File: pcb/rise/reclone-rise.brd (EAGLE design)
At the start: 85 x 56 mm, 130 parts, among them Y1 12MHz

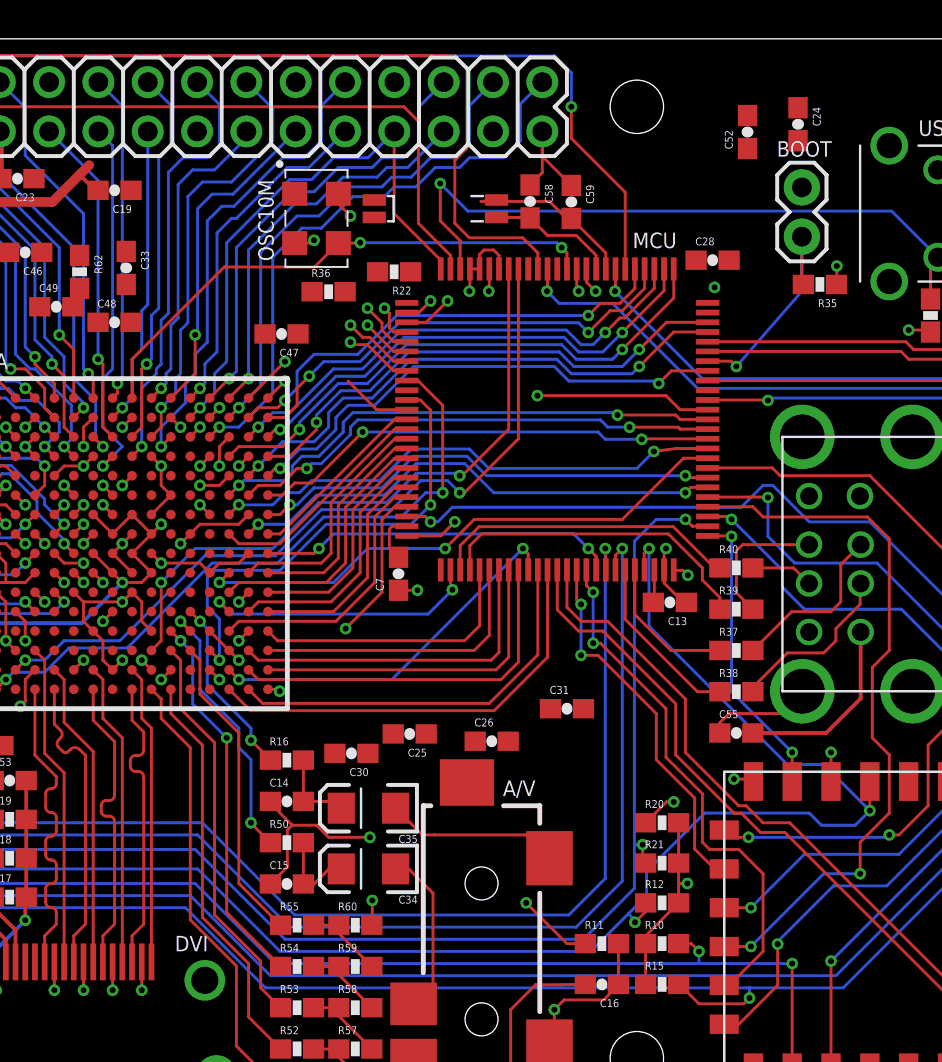
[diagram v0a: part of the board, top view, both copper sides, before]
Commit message: Placed and routed some pull resistors and bypass caps
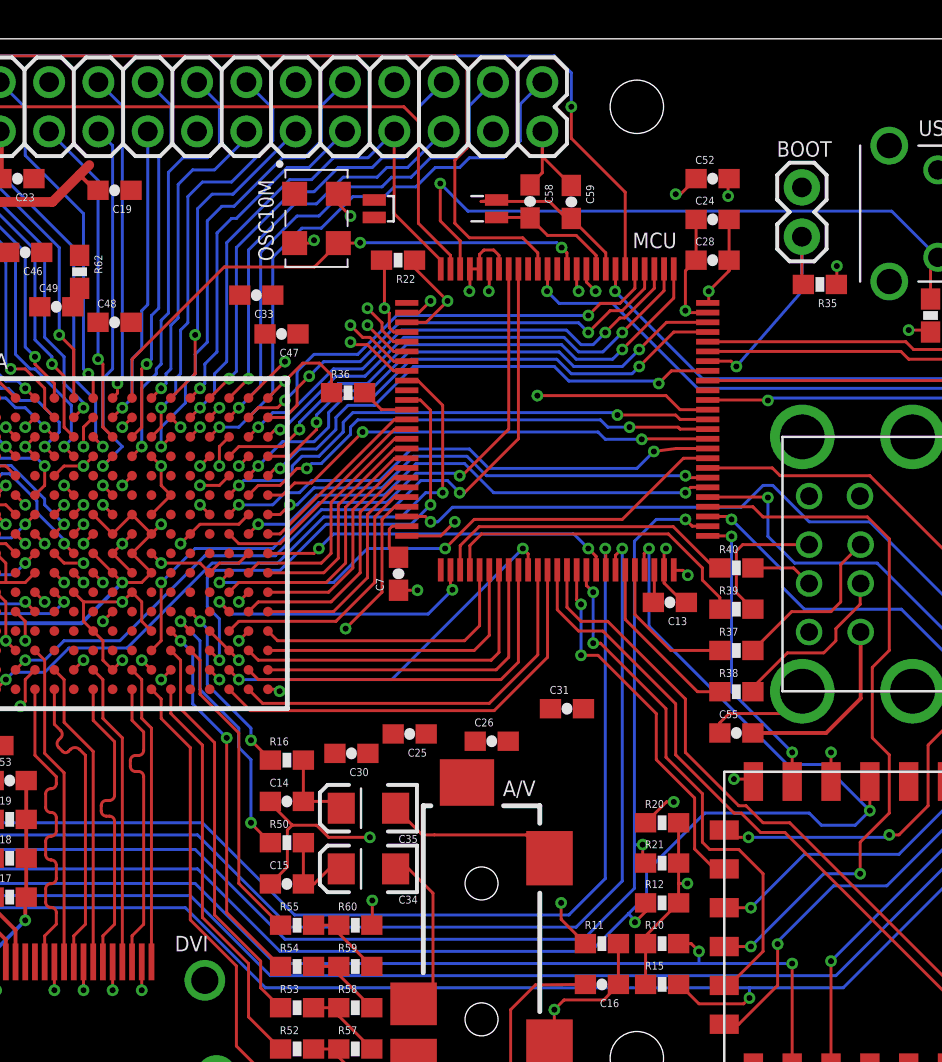
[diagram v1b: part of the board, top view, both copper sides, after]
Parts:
- moved C33 6.84 mm to (41.9, 42.8), turned to 180 degrees
- moved C24 6.59 mm to (65.4, 46.7), turned to 0 degrees
- moved R36 5.30 mm to (46.6, 37.8)
- moved C52 3.00 mm to (65.4, 48.8), turned to 0 degrees
- moved R22 0.63 mm to (49.2, 44.6)
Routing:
- net GND: track 171.4 -> 182.9 mm, vias 59 -> 61
- net +3V3: track 87.6 -> 95.0 mm
- net JTAG_TCK: track 112.9 -> 108.5 mm
- net SD_CS: track 57.6 -> 60.1 mm
- net +5V: track 208.8 -> 210.5 mm, vias 2 -> 3
- net BOOT1: track 3.64 -> 2.54 mm

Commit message: Almost done routing
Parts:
- moved C18 63.9 mm to (82.5, 38.0)
- moved C55 54.6 mm to (19.4, 47.7)
- moved C50 26.7 mm to (37.6, 18.0), turned to 90 degrees
- moved C38 19.0 mm to (21.5, 22.6)
- moved C49 18.8 mm to (24.6, 24.7), turned to 180 degrees
- moved C31 8.89 mm to (66.6, 19.8)
- moved C19 7.81 mm to (26.8, 47.8), turned to 90 degrees
- moved C26 7.56 mm to (46.5, 20.6), turned to 180 degrees
- moved C30 6.96 mm to (49.0, 25.8), turned to 0 degrees
- moved C46 6.08 mm to (36.0, 46.0)
- moved R62 5.86 mm to (27.5, 41.5), turned to 180 degrees
- moved C42 4.63 mm to (21.5, 24.7), turned to 0 degrees
- moved C43 4.48 mm to (20.8, 39.1)
- moved C25 3.71 mm to (46.5, 18.5)
- moved C45 3.42 mm to (24.6, 22.6), turned to 180 degrees
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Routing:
- net GND: track 182.9 -> 227.9 mm, vias 61 -> 76
- net +1V8: track 108.1 -> 134.8 mm
- net +3V3: track 95.0 -> 118.8 mm
- net +5V: track 210.5 -> 196.1 mm, vias 3 -> 4
- net +1V2: track 50.7 -> 56.8 mm, vias 2 -> 4
- net DDR2_VREF: track 57.7 -> 60.6 mm
- net M3A0: track 27.8 -> 26.9 mm
- net M3A9: vias 0 -> 2

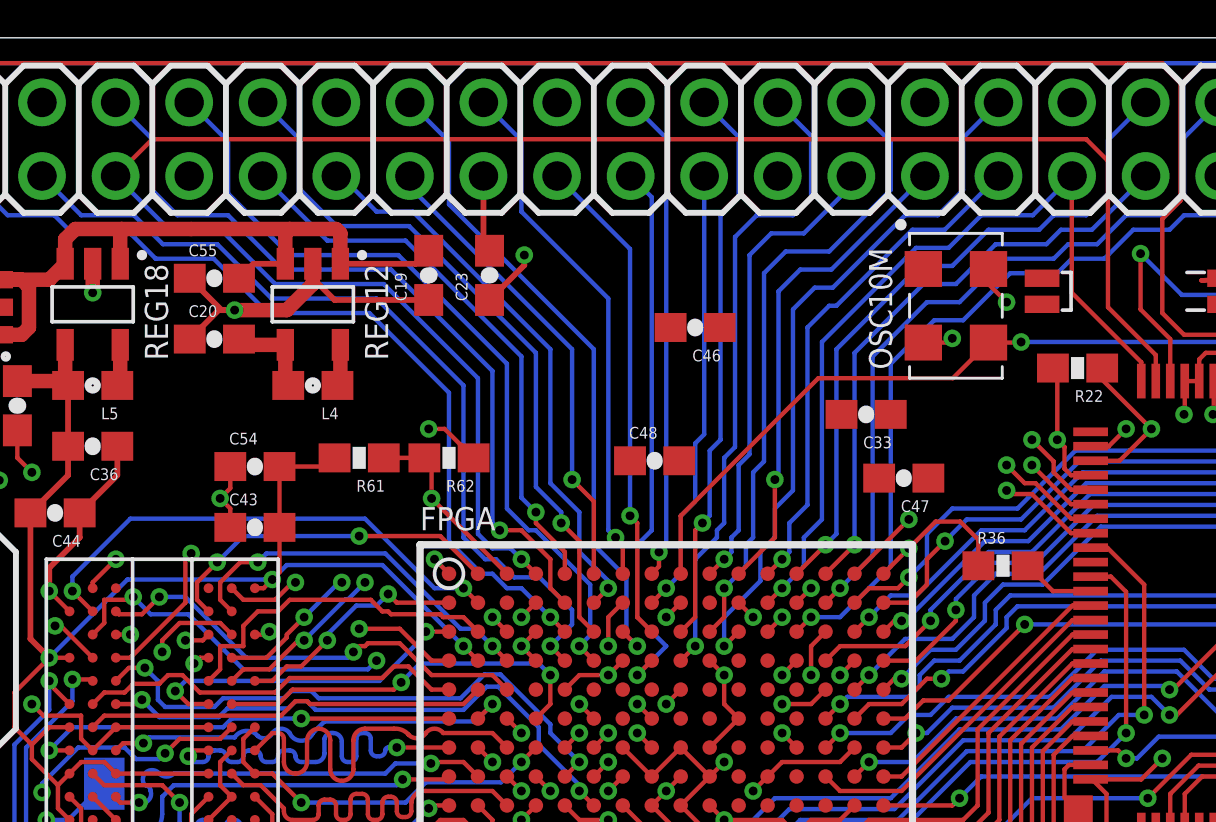
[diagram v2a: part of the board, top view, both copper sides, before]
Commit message: Finished routing first draft
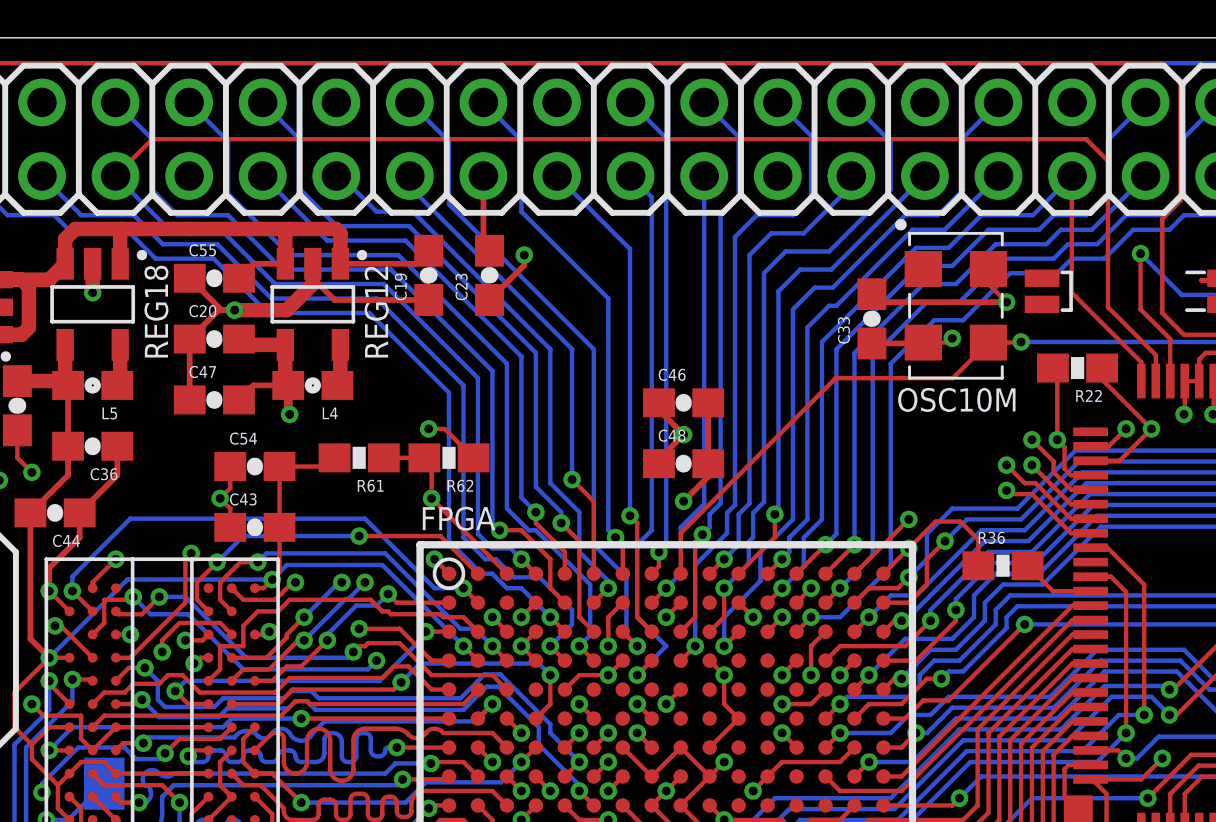
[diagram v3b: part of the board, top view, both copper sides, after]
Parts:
- moved C47 24.0 mm to (19.4, 43.5), turned to 0 degrees
- moved C33 3.31 mm to (42.1, 46.3), turned to 90 degrees
- moved C46 2.63 mm to (35.6, 43.4), turned to 0 degrees
- moved C48 1.00 mm to (35.6, 41.3)
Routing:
- net +1V2: track 56.8 -> 76.1 mm, vias 4 -> 6
- net GND: track 227.9 -> 234.6 mm, vias 76 -> 77
- net +3V3: track 118.8 -> 123.6 mm

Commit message: Fixed a few ERC issues
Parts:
- BAT: value (none) -> 3V
- BOOT: value (none) -> BOOT
- BUSPWR: value (none) -> BUSPWR
- Y4: value (none) -> 32K768
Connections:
- net GPIO25: now also FPGA.D12
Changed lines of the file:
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@@
 <element name="C7" library="SparkFun-Passives" package="0603-CAP" value="2u2" x="49.225" y="28.45" rot="R90"/>
 <element name="C13" library="SparkFun-Passives" package="0603-CAP" value="2u2" x="63.2" y="26.975" rot="R180"/>
-<element name="BOOT" library="SparkFun-Connectors" package="1X02" value="" x="70" y="48.35" locked="yes" smashed="yes" rot="R270">
+<element name="BOOT" library="SparkFun-Connectors" package="1X02" value="BOOT" x="70" y="48.35" locked="yes" smashed="yes" rot="R270">
 <attribute name="NAME" x="68.7038" y="49.9288" size="0.8" layer="25" font="vector" ratio="19"/>
 <attribute name="VALUE" x="66.825" y="49.62" size="1.27" layer="27" rot="R270"/>
 </element>
-<element name="BUSPWR" library="SparkFun-Connectors" package="1X02" value="" x="2" y="20" smashed="yes">
+<element name="BUSPWR" library="SparkFun-Connectors" package="1X02" value="BUSPWR" x="2" y="20" smashed="yes">
 <attribute name="NAME" x="0.6538" y="21.6288" size="0.8" layer="25" font="vector" ratio="19"/>
 <attribute name="VALUE" x="0.73" y="16.825" size="1.27" layer="27"/>
@@
 <element name="C54" library="SparkFun-Passives" package="0603-CAP" value="4u7" x="20.8" y="41.2"/>
 <element name="C55" library="SparkFun-Passives" package="0603-CAP" value="4u7" x="19.4" y="47.7"/>
-<element name="BAT" library="SparkFun-Electromechanical" package="BATTCON_12MM" value="" x="6.2" y="35.2" locked="yes" rot="R90">
+<element name="BAT" library="SparkFun-Electromechanical" package="BATTCON_12MM" value="3V" x="6.2" y="35.2" locked="yes" rot="R90">
 <attribute name="PROD_ID" value="BATT-08044" x="6.2" y="35.2" size="1.778" layer="27" rot="R90" display="off"/>
 </element>
-<element name="Y4" library="SparkFun-FreqCtrl" package="CRYSTAL-32KHZ-SMD_EPSON_MC146" value="" x="54.875" y="48" rot="R180"/>
+<element name="Y4" library="SparkFun-FreqCtrl" package="CRYSTAL-32KHZ-SMD_EPSON_MC146" value="32K768" x="54.875" y="48" rot="R180"/>
 <element name="C58" library="SparkFun-Passives" package="0603-CAP" value="6p8" x="56" y="47.625" rot="R270"/>
 <element name="C59" library="SparkFun-Passives" package="0603-CAP" value="6p8" x="58.125" y="47.6" rot="R270"/>
@@
 <contactref element="MCU" pad="21"/>
 <contactref element="MCU" pad="22"/>
-<contactref element="MCU" pad="100"/>
-<contactref element="MCU" pad="11"/>
-<contactref element="MCU" pad="19"/>
-<contactref element="MCU" pad="28"/>
-<contactref element="MCU" pad="50"/>
-<contactref element="MCU" pad="75"/>
 <contactref element="TXRX" pad="A"/>
 <contactref element="R15" pad="1"/>
@@
 <wire x1="17.375" y1="14.25" x2="19.7" y2="14.25" width="0.1524" layer="1"/>
 <wire x1="19.7" y1="14.25" x2="19.7001" y2="14.2501" width="0.1524" layer="1"/>
-<via x="64.125" y="28.375" extent="1-16" drill="0.3048" shape="octagon"/>
-<wire x1="63.4" y1="28.65" x2="63.425" y2="28.625" width="0.1524" layer="1"/>
 <via x="66.5" y="17.875" extent="1-16" drill="0.3048" shape="octagon"/>
 <wire x1="67.5" y1="17.75" x2="67.375" y2="17.875" width="0.1524" layer="1"/>
@@
 <wire x1="53.625" y1="45.125" x2="54.125" y2="45.125" width="0.1524" layer="1"/>
 <wire x1="54.125" y1="45.125" x2="54.4" y2="44.85" width="0.1524" layer="1"/>
-<wire x1="54.4" y1="44.85" x2="54.4" y2="44.15" width="0.1524" layer="1"/>
-<via x="58.5" y="43" extent="1-16" drill="0.3048" shape="octagon"/>
 <wire x1="39.5" y1="28.5" x2="39" y2="29" width="0.1524" layer="1"/>
 <wire x1="39" y1="29" x2="37" y2="29" width="0.1524" layer="1"/>
-<wire x1="58.4" y1="44.15" x2="58.4" y2="43.1" width="0.1524" layer="1"/>
-<wire x1="58.4" y1="43.1" x2="58.5" y2="43" width="0.1524" layer="1"/>
 <contactref element="OSC10M" pad="4"/>
 <via x="46.75" y="46.875" extent="1-16" drill="0.3048" shape="octagon"/>
@@
 <via x="41" y="25" extent="1-16" drill="0.3048" shape="octagon"/>
 <wire x1="41.5" y1="25.5" x2="41" y2="25" width="0.1524" layer="1"/>
-<via x="52.125" y="31.125" extent="1-16" drill="0.3048" shape="octagon"/>
-<wire x1="49.65" y1="30.4" x2="51.4" y2="30.4" width="0.1524" layer="1"/>
-<wire x1="51.4" y1="30.4" x2="52.125" y2="31.125" width="0.1524" layer="1"/>
 <via x="29.75" y="21.625" extent="1-16" drill="0.3048" shape="octagon"/>
 <wire x1="30.5" y1="23.5" x2="30" y2="23" width="0.1524" layer="1"/>
@@
 <wire x1="39.5" y1="31.5" x2="39" y2="32" width="0.1524" layer="1"/>
 <wire x1="41.5" y1="34.5" x2="41" y2="34" width="0.1524" layer="1"/>
-<wire x1="49.65" y1="41.4" x2="50.65" y2="41.4" width="0.1524" layer="1"/>
 <wire x1="50.65" y1="41.4" x2="51.75" y2="42.5" width="0.1524" layer="1"/>
-<wire x1="63.425" y1="28.625" x2="63.875" y2="28.625" width="0.1524" layer="1"/>
-<wire x1="63.875" y1="28.625" x2="64.125" y2="28.375" width="0.1524" layer="1"/>
 <via x="33" y="31" extent="1-16" drill="0.3048" shape="octagon"/>
 <wire x1="32.5" y1="30.5" x2="33" y2="31" width="0.1524" layer="1"/>
@@
 <wire x1="71.775" y1="43.35" x2="71.8" y2="43.375" width="0.1524" layer="1"/>
 <wire x1="71.8" y1="43.375" x2="71.8" y2="44.3" width="0.1524" layer="1"/>
-<wire x1="65.15" y1="42.4" x2="65.2" y2="42.45" width="0.1524" layer="1"/>
-<wire x1="65.2" y1="42.45" x2="65.2" y2="43" width="0.1524" layer="1"/>
+<wire x1="65.2" y1="42.4" x2="65.2" y2="43" width="0.1524" layer="1"/>
 <wire x1="66.25" y1="44.6" x2="66.25" y2="44.05" width="0.1524" layer="1"/>
 <wire x1="66.25" y1="44.05" x2="65.2" y2="43" width="0.1524" layer="1"/>
@@
 <wire x1="50.2" y1="28.8" x2="50.2" y2="29.9" width="0.1524" layer="1"/>
 <wire x1="50.2" y1="29.9" x2="49.7" y2="30.4" width="0.1524" layer="1"/>
-<wire x1="49.7" y1="30.4" x2="49.65" y2="30.4" width="0.1524" layer="1"/>
 <wire x1="20.175" y1="9.525" x2="20.75" y2="9.525" width="0.1524" layer="1"/>
 <wire x1="20.75" y1="9.525" x2="21.25" y2="10.025" width="0.1524" layer="1"/>
 <wire x1="42.1" y1="47.15" x2="42.375" y2="46.875" width="0.2" layer="1"/>
 <wire x1="42.375" y1="46.875" x2="46.75" y2="46.875" width="0.2" layer="1"/>
+<contactref element="MCU" pad="100"/>
+<contactref element="MCU" pad="11"/>
+<contactref element="MCU" pad="19"/>
+<contactref element="MCU" pad="28"/>
+<contactref element="MCU" pad="50"/>
+<contactref element="MCU" pad="75"/>
+<via x="64.125" y="28.375" extent="1-16" drill="0.3048" shape="octagon"/>
+<wire x1="63.4" y1="28.65" x2="63.425" y2="28.625" width="0.1524" layer="1"/>
+<via x="58.5" y="43" extent="1-16" drill="0.3048" shape="octagon"/>
+<wire x1="58.4" y1="44.15" x2="58.4" y2="43.1" width="0.1524" layer="1"/>
+<wire x1="58.4" y1="43.1" x2="58.5" y2="43" width="0.1524" layer="1"/>
+<via x="52.125" y="31.125" extent="1-16" drill="0.3048" shape="octagon"/>
+<wire x1="49.7" y1="30.4" x2="51.4" y2="30.4" width="0.1524" layer="1"/>
+<wire x1="51.4" y1="30.4" x2="52.125" y2="31.125" width="0.1524" layer="1"/>
+<wire x1="63.425" y1="28.625" x2="63.875" y2="28.625" width="0.1524" layer="1"/>
+<wire x1="63.875" y1="28.625" x2="64.125" y2="28.375" width="0.1524" layer="1"/>
+<wire x1="54.4" y1="44.85" x2="54.4" y2="44.15" width="0.1524" layer="1"/>
+<wire x1="65.15" y1="42.4" x2="65.2" y2="42.4" width="0.1524" layer="1"/>
+<wire x1="49.7" y1="30.4" x2="49.65" y2="30.4" width="0.1524" layer="1"/>
+<wire x1="50.65" y1="41.4" x2="49.65" y2="41.4" width="0.1524" layer="1"/>
 </signal>
 <signal name="FPGA_CONFIG_CLK">
@@
 <signal name="GPIO25">
 <contactref element="GPIO" pad="37"/>
+<contactref element="FPGA" pad="D12"/>
+<wire x1="38.5" y1="34.5" x2="54.09" y2="51.23" width="0" layer="19" extent="1-1"/>
 </signal>
 <signal name="GPIO26">
